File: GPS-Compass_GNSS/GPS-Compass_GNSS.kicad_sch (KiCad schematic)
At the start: 28 parts, among them J1 Conn_01x08_Socket, J2 SMA_F, Q4 BC337, U10 BGA725L6E6327FTSA1, U11 TESEO-LIV3R

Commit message: GNSS update
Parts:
- R41: footprint Resistor_SMD:R_0805_2012Metric -> Resistor_SMD:R_0402_1005Metric

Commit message: GNSS update
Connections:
- net +3V3: now also J1.1 (Pin_1); no longer J1.2 (Pin_2)
- net GND: now also J1.8 (Pin_8); no longer J1.1 (Pin_1)
- net GNSS_RST: now also J1.7 (Pin_7); no longer J1.8 (Pin_8)
- net GNSS_RX: now also J1.3 (Pin_3); no longer J1.6 (Pin_6)
- net GNSS_TX: now also J1.2 (Pin_2); no longer J1.5 (Pin_5)
- net GNSS_WKP: now also J1.6 (Pin_6); no longer J1.7 (Pin_7)
- net SCL: now also J1.4 (Pin_4); no longer J1.3 (Pin_3)
- net SDA: now also J1.5 (Pin_5); no longer J1.4 (Pin_4)
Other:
- moved on the sheet: J1

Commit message: gnss module
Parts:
- removed AE1: Antenna, gps-compass_brd:ANT2525B00DT1516S, symbol Device:Antenna
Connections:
- net GNSS_RX: now also J1.2 (Pin_2); no longer J1.3 (Pin_3)
- net GNSS_TX: now also J1.3 (Pin_3); no longer J1.2 (Pin_2)
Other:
- note added: "BOARD CONNECTOR"
- moved on the sheet: D1, D6, J1, Q4, R29, R3, R33

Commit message: GNSS and Mian ocb
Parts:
- removed J1: Conn_01x08_Socket, Connector_PinSocket_2.54mm:PinSocket_1x08_P2.54mm_Horizontal, symbol Connector:Conn_01x08_Socket
- removed R1: 10k, Resistor_SMD:R_0805_2012Metric, symbol Device:R_Small
- added C1: 100n, Capacitor_SMD:C_0805_2012Metric, symbol Device:C_Small
- added H1, H2, H3: MountingHole_Pad, MountingHole:MountingHole_2.2mm_M2_Pad_Via, symbol Mechanical:MountingHole_Pad
- added H4: MountingHole_Pad, MountingHole:MountingHole_3.2mm_M3_Pad_Via, symbol Mechanical:MountingHole_Pad
- added J3: Conn_01x10_Socket, Connector_PinSocket_2.54mm:PinSocket_1x10_P2.54mm_Horizontal, symbol Connector:Conn_01x10_Socket
- added JP1: Jumper_2_Small_Open, Jumper:SolderJumper-2_P1.3mm_Open_RoundedPad1.0x1.5mm, symbol Jumper:Jumper_2_Small_Open
- added R4: 10k, Resistor_SMD:R_0805_2012Metric, symbol Device:R_Small
- added SW1: GNSS_RST, Button_Switch_SMD:SW_SPST_B3U-1000P, symbol Switch:SW_Push
- added TP1, TP2, TP3, TP4: TestPoint, TestPoint:TestPoint_Pad_D1.0mm, symbol Connector:TestPoint
- C15: value 100nF -> 100n
- C28, C30: value 120pF -> 120p
- C29: value 1nF -> 1n
- C31, C32: value 56nF -> 56n
- C33: value 10nF -> 10n
- L4: value 5.6nH -> 5.6n
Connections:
- net +3V3: now also J3.2 (Pin_2), R4.2
- net ANT_OFF: now also TP2.1
- net GND: now also C1.2, J3.1 (Pin_1), J3.10 (Pin_10), SW1.1
- net GNSS_PPS: now also TP3.1
- net GNSS_RST: now also C1.1, J3.8 (Pin_8), R4.1, SW1.2
- net GNSS_RX: now also J3.3 (Pin_3)
- net GNSS_TX: now also J3.4 (Pin_4)
- net GNSS_WKP: now also J3.7 (Pin_7), TP1.1
- net SCL: now also J3.5 (Pin_5)
- net SDA: now also J3.6 (Pin_6)
- net VCC_RF: now also TP4.1
- net VCC_GNSS: no longer names the net of C32.1, L5.2, U11.7 (VCC_IO), U11.8 (VCC)
- net VCC_GNSS: now also JP1.1 (A); no longer U11.6 (VBATT)
- new net: JP1.2 (B), U11.6 (VBATT)
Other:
- note added: "add ESD protection? VIA FENCE PITCH CALCULATIOn Calculate impedance for CPWG"
- note removed: "add ESD protection"
- moved on the sheet: D1, D6, Q4, R29, R3, R33

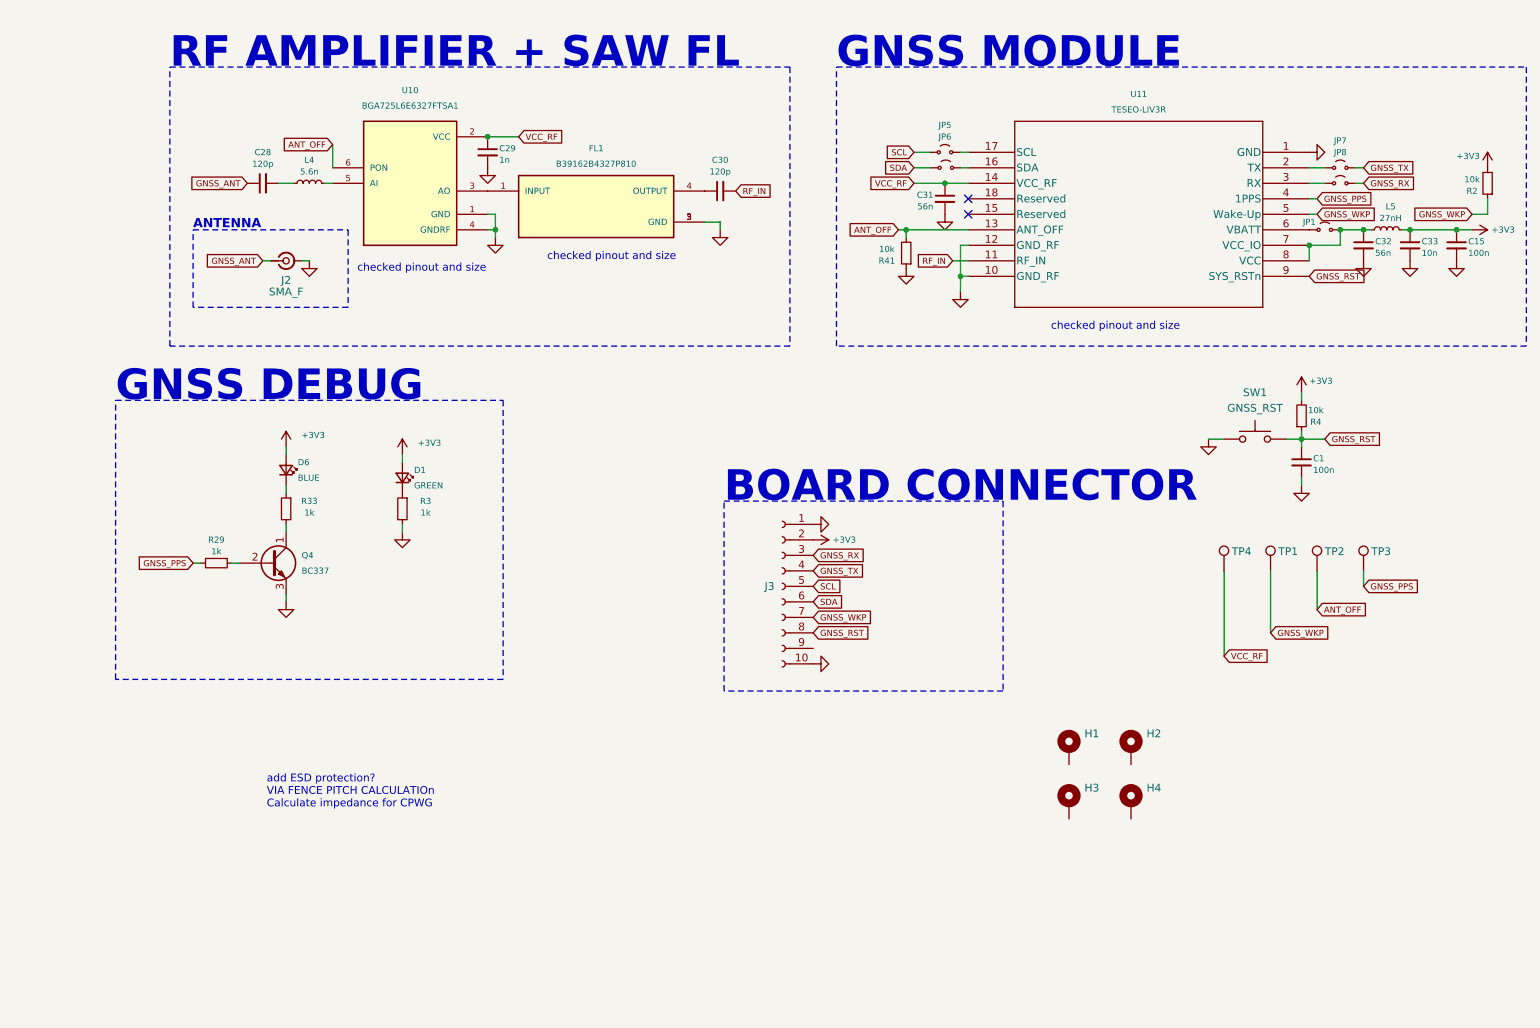
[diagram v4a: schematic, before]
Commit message: soldermask via fencing
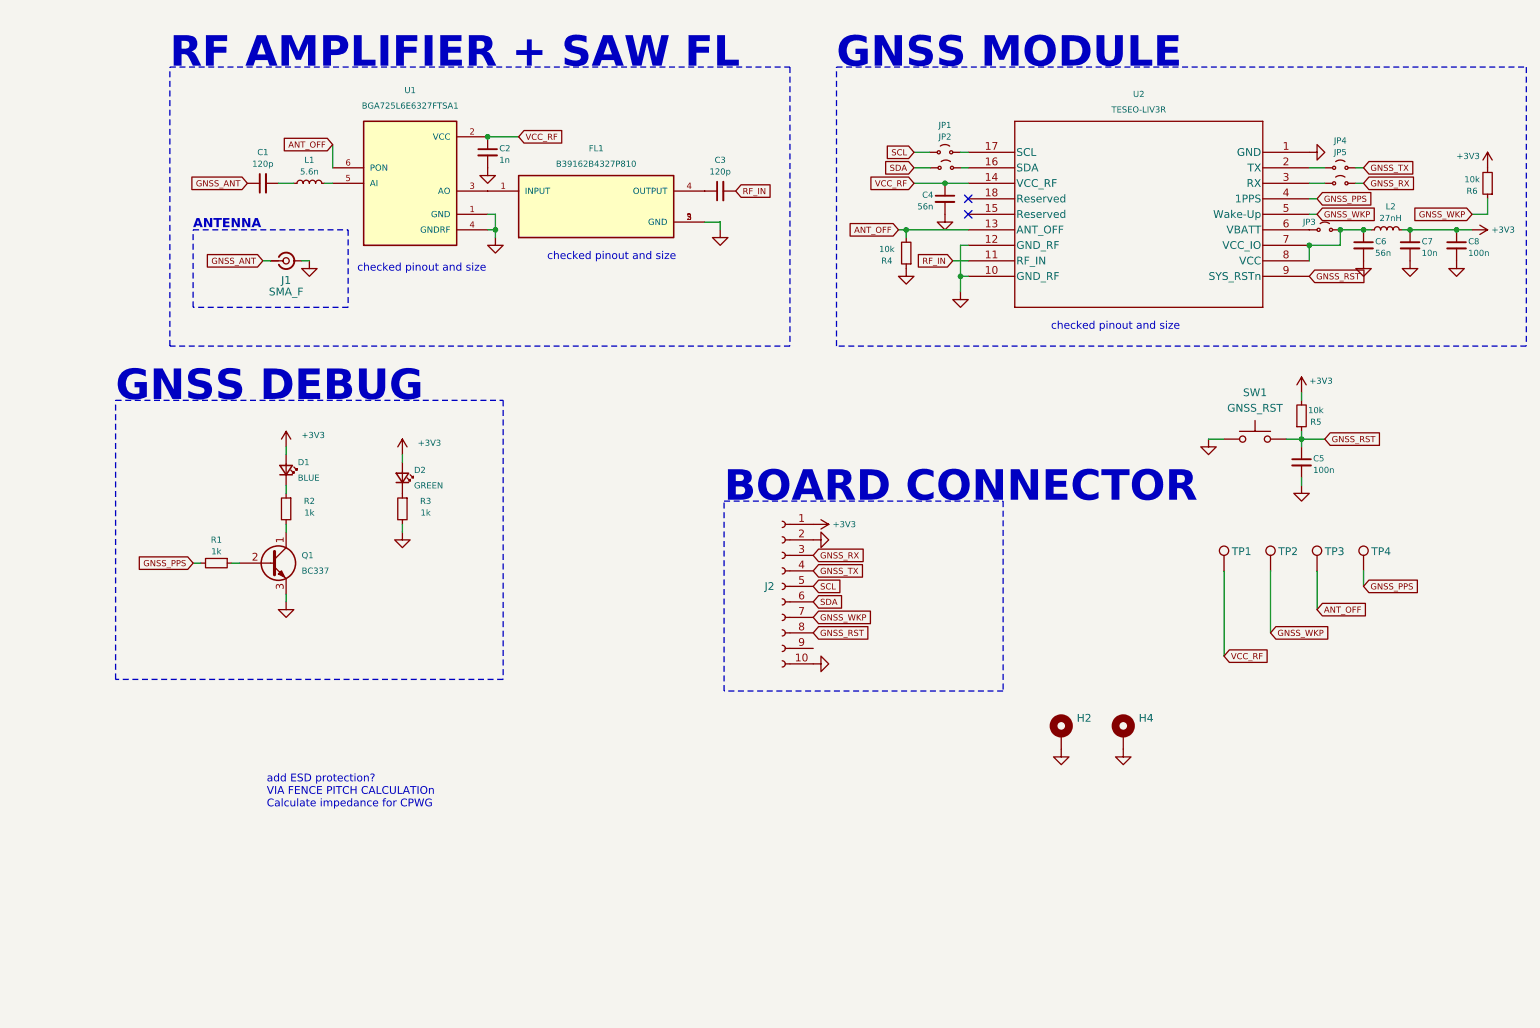
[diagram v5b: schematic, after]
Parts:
- removed H1, H2: MountingHole_Pad, MountingHole:MountingHole_2.2mm_M2_Pad_Via, symbol Mechanical:MountingHole_Pad
- H2: renamed from H3; footprint MountingHole:MountingHole_2.2mm_M2_Pad_Via -> MountingHole:MountingHole_3.2mm_M3
- H4: footprint MountingHole:MountingHole_3.2mm_M3_Pad_Via -> MountingHole:MountingHole_3.2mm_M3
- renumbered C28 to C1, C29 to C2, C30 to C3, C31 to C4, C1 to C5, C32 to C6, C33 to C7, C15 to C8, D6 to D1, D1 to D2, J2 to J1, J3 to J2, JP5 to JP1, JP6 to JP2, JP1 to JP3, JP7 to JP4, JP8 to JP5, L4 to L1, L5 to L2, Q4 to Q1, R29 to R1, R33 to R2, R41 to R4, R4 to R5, R2 to R6, TP4 to TP1, TP1 to TP2, TP2 to TP3, TP3 to TP4, U10 to U1, U11 to U2
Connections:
- net +3V3: now also J2.1 (Pin_1); no longer J2.2 (Pin_2)
- net GND: now also H2.1, H4.1, J2.2 (Pin_2); no longer J2.1 (Pin_1)
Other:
- moved on the sheet: H2, H4

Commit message: finished
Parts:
- removed JP3: Jumper_2_Small_Open, Jumper:SolderJumper-2_P1.3mm_Open_RoundedPad1.0x1.5mm, symbol Jumper:Jumper_2_Small_Open
- removed Q1: BC337, Package_TO_SOT_THT:TO-92_Inline, symbol Transistor_BJT:BC337
- added Q1: MMBT3904, Package_TO_SOT_SMD:SOT-23, symbol Transistor_BJT:MMBT3904
- renumbered H2 to H1, H4 to H2
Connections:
- net GND: now also J2.9 (Pin_9), Q1.2 (E)
- net GNSS_RST: now also J2.3 (Pin_3); no longer J2.8 (Pin_8)
- net GNSS_RX: now also J2.5 (Pin_5); no longer J2.3 (Pin_3)
- net GNSS_TX: now also J2.6 (Pin_6); no longer J2.4 (Pin_4)
- net GNSS_WKP: now also J2.4 (Pin_4); no longer J2.7 (Pin_7)
- net SCL: now also J2.7 (Pin_7); no longer J2.5 (Pin_5)
- net SDA: now also J2.8 (Pin_8); no longer J2.6 (Pin_6)
- net at C6.1, L2.2, U2.7 (VCC_IO)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: now also U2.6 (VBATT)
- net at R2.2: now also Q1.3 (C)
- net at R1.1: now also Q1.1 (B)
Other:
- note added: "1. 2. 3. 4. 5. 6. 7."
- note added: "BOARD CONN."
- note added: "MOUNTING"
- note added: "RESET"
- note added: "TEST POINTS"
- note added: "TO-DO LIST"
- note removed: "BOARD CONNECTOR"
- note removed: "add ESD protection? VIA FENCE PITCH CALCULATIOn Calculate impedance for CPWG"
- company: (none) -> SPS na Proseku
- title: (none) -> GNSS_Module
- moved on the sheet: C1, C2, C3, C4, C5, C6, C7, C8, D1, D2, FL1, H1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
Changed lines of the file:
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@@
 	(generator_version "9.0")
 	(paper "A4")
+	(title_block
+		(title "GNSS_Module")
+		(date "2025-08-26")
+		(rev "v1.0.0")
+		(company "SPS na Proseku")
+		(comment 1 "made by bismarx")
+		(comment 2 "GNSS module for GPS Compass project")
+	)

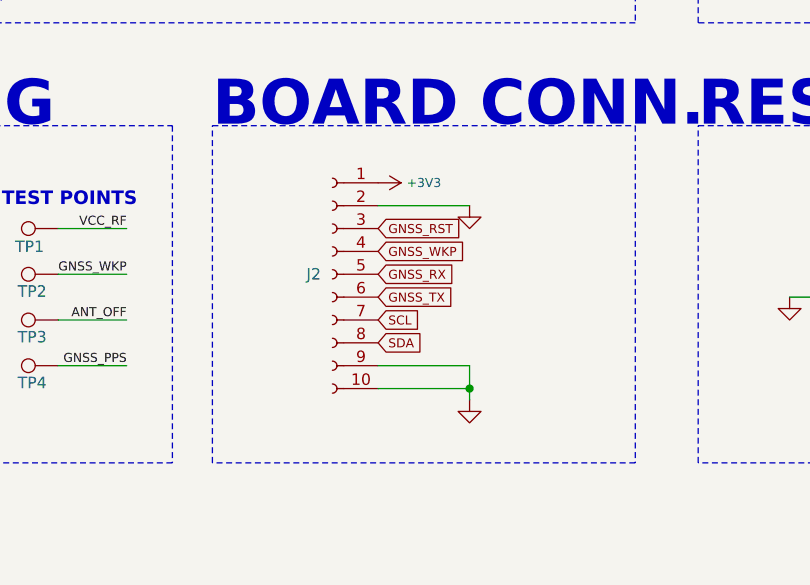
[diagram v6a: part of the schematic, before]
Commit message: changed socket to header for breadboard pluggablity
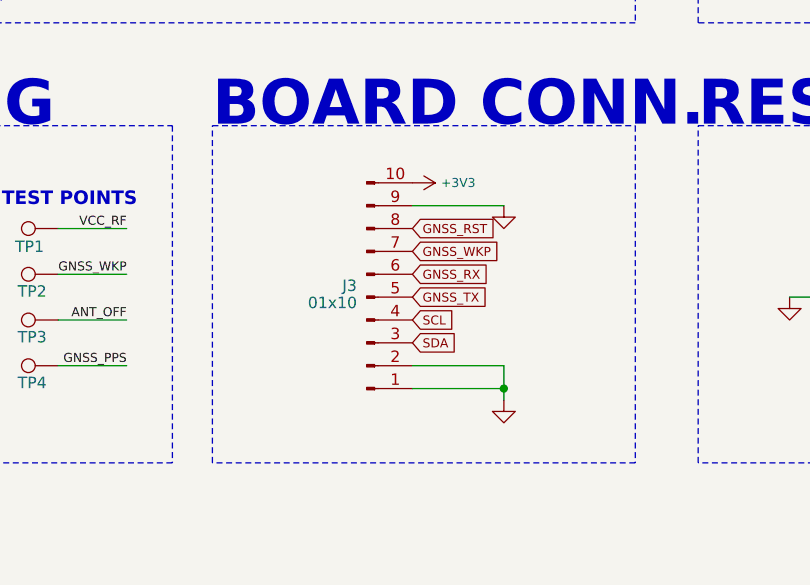
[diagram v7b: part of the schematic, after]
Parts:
- removed J2: Conn_01x10_Socket, Connector_PinSocket_2.54mm:PinSocket_1x10_P2.54mm_Horizontal, symbol Connector:Conn_01x10_Socket
- added J3: 01x10, Connector_PinHeader_2.54mm:PinHeader_1x10_P2.54mm_Horizontal, symbol Connector:Conn_01x10_Pin
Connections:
- net +3V3: now also J3.10 (Pin_10)
- net GND: now also J3.1 (Pin_1), J3.2 (Pin_2), J3.9 (Pin_9)
- net GNSS_RST: now also J3.8 (Pin_8)
- net GNSS_RX: now also J3.6 (Pin_6)
- net GNSS_TX: now also J3.5 (Pin_5)
- net GNSS_WKP: now also J3.7 (Pin_7)
- net SCL: now also J3.4 (Pin_4)
- net SDA: now also J3.3 (Pin_3)

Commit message: schematric remake
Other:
- moved on the sheet: C1, C6, C7, C8, J1, J3, JP4, JP5, L2, R6
